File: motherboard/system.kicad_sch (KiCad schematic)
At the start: 25 parts, among them J10 DEBUG UART, J11 PWR ON MODE, J12 5V FAN, J7 RTC BATTERY, Q10 2SK3018W, Q11 AO3415A, SW1 PWR, SW2 RESET, SW3 MASK, SW4 RECOVERY

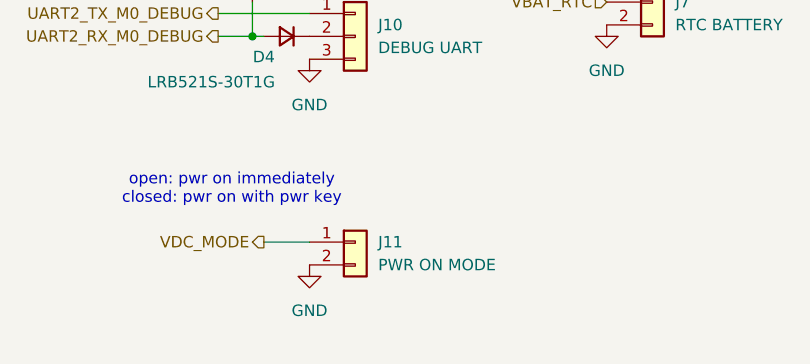
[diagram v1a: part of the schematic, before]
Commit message: linked all footprints
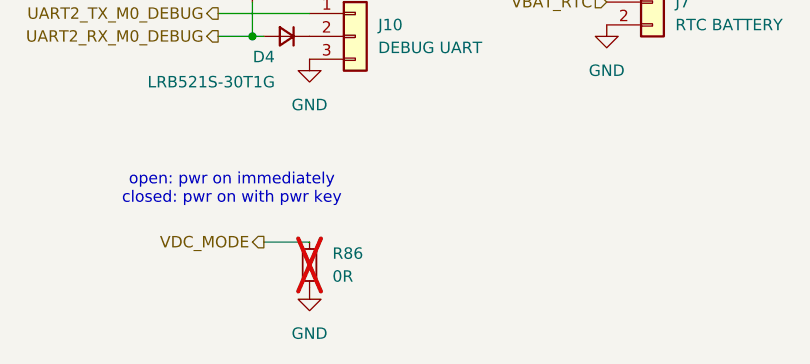
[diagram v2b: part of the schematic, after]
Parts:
- removed J11: PWR ON MODE, symbol Connector_Generic:Conn_01x02
- added R86: 0R, Resistor_SMD:R_0402_1005Metric, symbol Device:R_Small
- D4: footprint (none) -> Diode_SMD:D_SOD-523
- J10: footprint (none) -> Connector_PinHeader_2.54mm:PinHeader_1x03_P2.54mm_Vertical
- J12: footprint (none) -> Connector_PinHeader_2.54mm:PinHeader_1x02_P2.54mm_Vertical
- J7: footprint (none) -> Connector_RJ:RJ45_Wuerth_7499111446_Horizontal
- Q11: footprint (none) -> Package_TO_SOT_SMD:SOT-23
- R41, R42, R43, R44, R45, R46, R47, R48, R49: footprint (none) -> Resistor_SMD:R_0402_1005Metric
- SW1, SW2, SW3, SW4: footprint (none) -> Button_Switch_SMD:SW_Push_1P1T_XKB_TS-1187A
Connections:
- net GND: now also R86.2
- net VDC_MODE: now also R86.1
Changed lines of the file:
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@@
 			)
 		)
-		(property "Footprint" ""
+		(property "Footprint" "Resistor_SMD:R_0402_1005Metric"
 			(at 64.77 74.93 0)
 			(effects
@@
 			)
 		)
-		(property "Footprint" ""
+		(property "Footprint" "Diode_SMD:D_SOD-523"
 			(at 55.88 153.67 90)
 			(effects
@@
 			)
 		)
-		(property "Footprint" ""
+		(property "Footprint" "Resistor_SMD:R_0402_1005Metric"
 			(at 130.81 85.09 0)
 			(effects
@@
 			)
 		)
-		(property "Footprint" ""
+		(property "Footprint" "Resistor_SMD:R_0402_1005Metric"
 			(at 140.97 88.9 0)
 			(effects
@@
 	(symbol
 		(lib_id "power:GND")
-		(at 58.42 179.07 0)
+		(at 58.42 181.61 0)
 		(unit 1)
 		(exclude_from_sim no)
@@
 		(fields_autoplaced yes)
 		(property "Reference" "#PWR067"
-			(at 58.42 185.42 0)
+			(at 58.42 187.96 0)
 			(effects
 				(font
@@
 		)
 		(property "Value" "GND"
-			(at 58.42 184.15 0)
+			(at 58.42 186.69 0)
 			(effects
 				(font
@@
 		)
 		(property "Footprint" ""
-			(at 58.42 179.07 0)
+			(at 58.42 181.61 0)
 			(effects
 				(font
@@
 		)
 		(property "Datasheet" ""
-			(at 58.42 179.07 0)
+			(at 58.42 181.61 0)
 			(effects
 				(font
@@
 		)
 		(property "Description" "Power symbol creates a global label with name \"GND\" , ground"
-			(at 58.42 179.07 0)
+			(at 58.42 181.61 0)
 			(effects
 				(font
@@
 			)
 		)
-		(property "Footprint" ""
+		(property "Footprint" "Button_Switch_SMD:SW_Push_1P1T_XKB_TS-1187A"
 			(at 77.47 74.93 0)
 			(effects
@@
 			)
 		)
-		(property "Footprint" ""
+		(property "Footprint" "Resistor_SMD:R_0402_1005Metric"
 			(at 154.94 78.74 0)
 			(effects
@@
 			)
 		)
-		(property "Footprint" ""
+		(property "Footprint" "Button_Switch_SMD:SW_Push_1P1T_XKB_TS-1187A"
 			(at 77.47 106.68 0)
 			(effects
@@
 			)
 		)
-		(property "Footprint" ""
+		(property "Footprint" "Resistor_SMD:R_0402_1005Metric"
 			(at 64.77 57.15 0)
 			(effects
@@
 			)
 		)
-		(property "Footprint" ""
+		(property "Footprint" "Connector_PinHeader_2.54mm:PinHeader_1x02_P2.54mm_Vertical"
 			(at 191.77 64.77 0)
 			(effects
@@
 	)
 	(symbol
-		(lib_id "Connector_Generic:Conn_01x02")
-		(at 63.5 176.53 0)
-		(unit 1)
-		(exclude_from_sim no)
-		(in_bom yes)
-		(on_board yes)
-		(dnp no)
-		(fields_autoplaced yes)
-		(property "Reference" "J11"
-			(at 66.04 176.5299 0)
-			(effects
-				(font
-					(size 1.27 1.27)
-				)
-				(justify left)
-			)
-		)
-		(property "Value" "PWR ON MODE"
-			(at 66.04 179.0699 0)
-			(effects
-				(font
-					(size 1.27 1.27)
-				)
-				(justify left)
-			)
-		)
-		(property "Footprint" ""
-			(at 63.5 176.53 0)
-			(effects
-				(font
-					(size 1.27 1.27)
-				)
-				(hide yes)
-			)
-		)
-		(property "Datasheet" "~"
-			(at 63.5 176.53 0)
-			(effects
-				(font
-					(size 1.27 1.27)
-				)
-				(hide yes)
-			)
-		)
-		(property "Description" "Generic connector, single row, 01x02, script generated (kicad-library-utils/schlib/autogen/connector/)"
-			(at 63.5 176.53 0)
-			(effects
-				(font
-					(size 1.27 1.27)
-				)
-				(hide yes)
-			)
-		)
-		(pin "2"
-		)
-		(pin "1"
-		)
-		(instances
-			(project "motherboard"
-				(path "/025fe4d1-0305-4b34-be04-f8d9818125a4/d2371120-9201-4f7f-a684-821b8780a78d"
-					(reference "J11")
-					(unit 1)
-				)
-			)
-		)
-	)
-	(symbol
 		(lib_id "Device:R_Small")
 		(at 64.77 106.68 90)
@@
 			)
 		)
-		(property "Footprint" ""
+		(property "Footprint" "Resistor_SMD:R_0402_1005Metric"
 			(at 64.77 106.68 0)
 			(effects
@@
 			)
 		)
-		(property "Footprint" ""
+		(property "Footprint" "Resistor_SMD:R_0402_1005Metric"
 			(at 64.77 90.17 0)
 			(effects
@@
 			)
 		)
-		(property "Footprint" ""
+		(property "Footprint" "Button_Switch_SMD:SW_Push_1P1T_XKB_TS-1187A"
 			(at 77.47 57.15 0)
 			(effects
@@
 	)
 	(symbol
+		(lib_id "Device:R_Small")
+		(at 58.42 179.07 0)
+		(unit 1)
+		(exclude_from_sim no)
+		(in_bom yes)
+		(on_board yes)
+		(dnp yes)
+		(fields_autoplaced yes)
+		(property "Reference" "R86"
+			(at 60.96 177.7999 0)
+			(effects
+				(font
+					(size 1.27 1.27)
+				)
+				(justify left)
+			)
+		)
+		(property "Value" "0R"
+			(at 60.96 180.3399 0)
+			(effects
+				(font
+					(size 1.27 1.27)
+				)
+				(justify left)
+			)
+		)
+		(property "Footprint" "Resistor_SMD:R_0402_1005Metric"
+			(at 58.42 179.07 0)
+			(effects
+				(font
+					(size 1.27 1.27)
+				)
+				(hide yes)
+			)
+		)
+		(property "Datasheet" "~"
+			(at 58.42 179.07 0)
+			(effects
+				(font
+					(size 1.27 1.27)
+				)
+				(hide yes)
+			)
+		)
+		(property "Description" "Resistor, small symbol"
+			(at 58.42 179.07 0)
+			(effects
+				(font
+					(size 1.27 1.27)
+				)
+				(hide yes)
+			)
+		)
+		(pin "2"
+		)
+		(pin "1"
+		)
+		(instances
+			(project ""
+				(path "/025fe4d1-0305-4b34-be04-f8d9818125a4/d2371120-9201-4f7f-a684-821b8780a78d"
+					(reference "R86")
+					(unit 1)
+				)
+			)
+		)
+	)
+	(symbol
 		(lib_id "power:GND")
 		(at 53.34 80.01 0)
@@
 			)
 		)
-		(property "Footprint" ""
+		(property "Footprint" "Connector_RJ:RJ45_Wuerth_7499111446_Horizontal"
 			(at 96.52 149.86 0)
 			(effects
@@
 			)
 		)
-		(property "Footprint" ""
+		(property "Footprint" "Connector_PinHeader_2.54mm:PinHeader_1x03_P2.54mm_Vertical"
 			(at 63.5 153.67 0)
 			(effects
@@
 			)
 		)
-		(property "Footprint" ""
+		(property "Footprint" "Button_Switch_SMD:SW_Push_1P1T_XKB_TS-1187A"
 			(at 77.47 90.17 0)
 			(effects
@@
 			)
 		)
-		(property "Footprint" ""
+		(property "Footprint" "Resistor_SMD:R_0402_1005Metric"
 			(at 142.24 72.39 0)
 			(effects
@@
 			)
 		)
-		(property "Footprint" ""
+		(property "Footprint" "Resistor_SMD:R_0402_1005Metric"
 			(at 166.37 64.77 0)
 			(effects
@@
 			)
 		)
-		(property "Footprint" ""
+		(property "Footprint" "Package_TO_SOT_SMD:SOT-23"
 			(at 157.48 62.23 0)
 			(effects

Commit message: cost optimizations for jlc
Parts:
- R49: footprint Resistor_SMD:R_0402_1005Metric -> Resistor_SMD:R_0603_1608Metric
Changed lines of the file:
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@@
 			)
 		)
-		(property "Description" "Unpolarized capacitor, small symbol"
+		(property "Description" "C527590"
 			(at 173.99 67.31 0)
 			(effects
@@
 			)
 		)
-		(property "Footprint" "Resistor_SMD:R_0402_1005Metric"
+		(property "Footprint" "Resistor_SMD:R_0603_1608Metric"
 			(at 166.37 64.77 0)
 			(effects

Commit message: audio done
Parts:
- added C70: 0.1uF, Capacitor_SMD:C_0402_1005Metric, symbol Device:C_Small
- added U24: SOT23 Hall Effect Sensor, Package_TO_SOT_SMD:SOT-23, symbol Sensor_Magnetic:SM351LT
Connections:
- net +3.3V: now also C70.1, U24.1 (VCC)
- net GND: now also C70.2, U24.3 (GND)
- new net GPIO4_C2/HALL_OUT: U24.2 (OUTPUT)

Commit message: motherboard schematic done
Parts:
- added C90: 0.1uF, Capacitor_SMD:C_0402_1005Metric, symbol Device:C_Small
- added C91: 1uF, Capacitor_SMD:C_0402_1005Metric, symbol Device:C_Small
- added R116, R117: 10k, Resistor_SMD:R_0402_1005Metric, symbol Device:R_Small
- added U28: SPI Flash, Package_SO:SOIC-8_3.9x4.9mm_P1.27mm, symbol Memory_Flash:AT25SF081-SSHF-X
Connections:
- net +3.3V: now also C90.1, C91.1, R116.1, R117.1, U28.8 (VCC)
- net GND: now also C90.2, C91.2, U28.4 (GND)
- new net FSPI_CLK: U28.6 (SCK)
- new net FSPI_CSN0: U28.1 (~{CS})
- new net FSPI_D0: U28.5 (SI/IO0)
- new net FSPI_D1: U28.2 (SO/IO1)
- new net FSPI_D2: R116.2, U28.3 (~{WP}/IO2)
- new net FSPI_D3: R117.2, U28.7 (~{HOLD}/IO3)
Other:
- note added: "might be needed to enable nvme boot"
- moved on the sheet: C32, C70, J12, Q10, Q11, R45, R46, R47, R48, R49, U24

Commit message: work preparing for routing
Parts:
- added J11: SYSTEM, 6P_05mm_FPC:FPC-SMD_6P-P0.50_XUNPU_FPC-05F-6PH20, symbol Connector_Generic_MountingPin:Conn_01x06_MountingPin
- J7: footprint Connector_RJ:RJ45_Wuerth_7499111446_Horizontal -> Connector_PinHeader_2.54mm:PinHeader_1x02_P2.54mm_Horizontal
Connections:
- net +3.3V: now also J11.2 (Pin_2)
- net GND: now also J11.1 (Pin_1), J11.MP (MountPin)
- net PWRON_L: now also R41.2, SW1.1 (A), J11.6 (Pin_6)
- net RECOVERY: now also R44.2, SW4.1 (A)
- net RESET_L: now also R42.2, SW2.1 (A), J11.5 (Pin_5)
- net UART2_TX_M0_DEBUG: now also J11.3 (Pin_3)
- net BOOT_SARADC: now reaches R43.2, SW3.1 (A)
- net BOOT_SARADC: now also J11.4 (Pin_4)
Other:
- moved on the sheet: SW1, SW2, SW3, SW4

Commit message: layout nearing completion
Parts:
- removed J7: RTC BATTERY, Connector_PinHeader_2.54mm:PinHeader_1x02_P2.54mm_Horizontal, symbol Connector_Generic:Conn_01x02
- C32: footprint Capacitor_SMD:C_0402_1005Metric -> Capacitor_SMD:C_0603_1608Metric
- R86: footprint Resistor_SMD:R_0402_1005Metric -> Jumper:SolderJumper-2_P1.3mm_Open_TrianglePad1.0x1.5mm
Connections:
- net PWRON_L: no longer J11.6 (Pin_6), R41.2, SW1.1 (A)
- net RECOVERY: no longer R44.2, SW4.1 (A)
- net RESET_L: no longer J11.5 (Pin_5), R42.2, SW2.1 (A)
- new net PWRON_L_IN: J11.6 (Pin_6), R41.2, SW1.1 (A)
- new net RECOVERY_IN: R44.2, SW4.1 (A)
- new net RESET_L_IN: J11.5 (Pin_5), R42.2, SW2.1 (A)
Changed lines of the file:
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@@
 		)
 	)
-	(label "PWRON_L"
+	(label "PWRON_L_IN"
 		(at 68.58 57.15 0)
 		(fields_autoplaced yes)
@@
 		)
 	)
-	(label "RESET_L"
+	(label "RESET_L_IN"
 		(at 107.95 82.55 0)
 		(fields_autoplaced yes)
@@
 		)
 	)
-	(label "RESET_L"
+	(label "RESET_L_IN"
 		(at 68.58 74.93 0)
 		(fields_autoplaced yes)
@@
 		)
 	)
-	(label "RECOVERY"
+	(label "RECOVERY_IN"
 		(at 68.58 106.68 0)
 		(fields_autoplaced yes)
@@
 		)
 	)
-	(label "PWRON_L"
+	(label "PWRON_L_IN"
 		(at 107.95 80.01 0)
 		(fields_autoplaced yes)
@@
 		)
 	)
-	(hierarchical_label "VBAT_RTC"
-		(shape input)
-		(at 91.44 149.86 180)
-		(fields_autoplaced yes)
-		(effects
-			(font
-				(size 1.27 1.27)
-			)
-			(justify right)
-		)
-	)
 	(symbol
 		(lib_id "Device:R_Small")
@@
 			)
 		)
-		(property "Footprint" "Capacitor_SMD:C_0402_1005Metric"
+		(property "Footprint" "Capacitor_SMD:C_0603_1608Metric"
 			(at 170.18 31.75 0)
 			(effects
@@
 			)
 		)
-		(property "Footprint" "Resistor_SMD:R_0402_1005Metric"
+		(property "Footprint" "Jumper:SolderJumper-2_P1.3mm_Open_TrianglePad1.0x1.5mm"
 			(at 58.42 179.07 0)
 			(effects
@@
 	)
 	(symbol
-		(lib_id "Connector_Generic:Conn_01x02")
-		(at 96.52 149.86 0)
-		(unit 1)
-		(exclude_from_sim no)
-		(in_bom yes)
-		(on_board yes)
-		(dnp no)
-		(fields_autoplaced yes)
-		(property "Reference" "J7"
-			(at 99.06 149.8599 0)
-			(effects
-				(font
-					(size 1.27 1.27)
-				)
-				(justify left)
-			)
-		)
-		(property "Value" "RTC BATTERY"
-			(at 99.06 152.3999 0)
-			(effects
-				(font
-					(size 1.27 1.27)
-				)
-				(justify left)
-			)
-		)
-		(property "Footprint" "Connector_PinHeader_2.54mm:PinHeader_1x02_P2.54mm_Horizontal"
-			(at 96.52 149.86 0)
-			(effects
-				(font
-					(size 1.27 1.27)
-				)
-				(hide yes)
-			)
-		)
-		(property "Datasheet" "~"
-			(at 96.52 149.86 0)
-			(effects
-				(font
-					(size 1.27 1.27)
-				)
-				(hide yes)
-			)
-		)
-		(property "Description" "Generic connector, single row, 01x02, script generated (kicad-library-utils/schlib/autogen/connector/)"
-			(at 96.52 149.86 0)
-			(effects
-				(font
-					(size 1.27 1.27)
-				)
-				(hide yes)
-			)
-		)
-		(pin "2"
-		)
-		(pin "1"
-		)
-		(instances
-			(project "motherboard"
-				(path "/025fe4d1-0305-4b34-be04-f8d9818125a4/d2371120-9201-4f7f-a684-821b8780a78d"
-					(reference "J7")
-					(unit 1)
-				)
-			)
-		)
-	)
-	(symbol
 		(lib_id "Connector_Generic:Conn_01x03")
 		(at 63.5 153.67 0)
@@
 					(unit 1)
 				)
-			)
-		)
-	)
-	(symbol
-		(lib_id "power:GND")
-		(at 91.44 152.4 0)
-		(unit 1)
-		(exclude_from_sim no)
-		(in_bom yes)
-		(on_board yes)
-		(dnp no)
-		(fields_autoplaced yes)
-		(property "Reference" "#PWR064"
-			(at 91.44 158.75 0)
-			(effects
-				(font
-					(size 1.27 1.27)
-				)
-				(hide yes)
-			)
-		)
-		(property "Value" "GND"
-			(at 91.44 157.48 0)
-			(effects
-				(font
-					(size 1.27 1.27)
-				)
-			)
-		)
-		(property "Footprint" ""
-			(at 91.44 152.4 0)
-			(effects
-				(font
-					(size 1.27 1.27)
-				)
-				(hide yes)
-			)
-		)
-		(property "Datasheet" ""
-			(at 91.44 152.4 0)
-			(effects
-				(font
-					(size 1.27 1.27)
-				)
-				(hide yes)
-			)
-		)
-		(property "Description" "Power symbol creates a global label with name \"GND\" , ground"
-			(at 91.44 152.4 0)
-			(effects
-				(font
-					(size 1.27 1.27)
-				)
-				(hide yes)
-			)
-		)
-		(pin "1"
-		)
-		(instances
-			(project "motherboard"
-				(path "/025fe4d1-0305-4b34-be04-f8d9818125a4/d2371120-9201-4f7f-a684-821b8780a78d"
-					(reference "#PWR064")
-					(unit 1)
-				)
